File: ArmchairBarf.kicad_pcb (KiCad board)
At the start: 2 copper layers, 33 x 20.3 mm, 12 parts, among them J1 Conn_01x03_Socket, U1 WS2812-2020, U2 WS2812-2020, U3 WS2812-2020, U4 WS2812-2020, U5 WS2812-2020, U6 WS2812-2020, U7 WS2812-2020, U8 WS2812-2020, U9 WS2812-2020

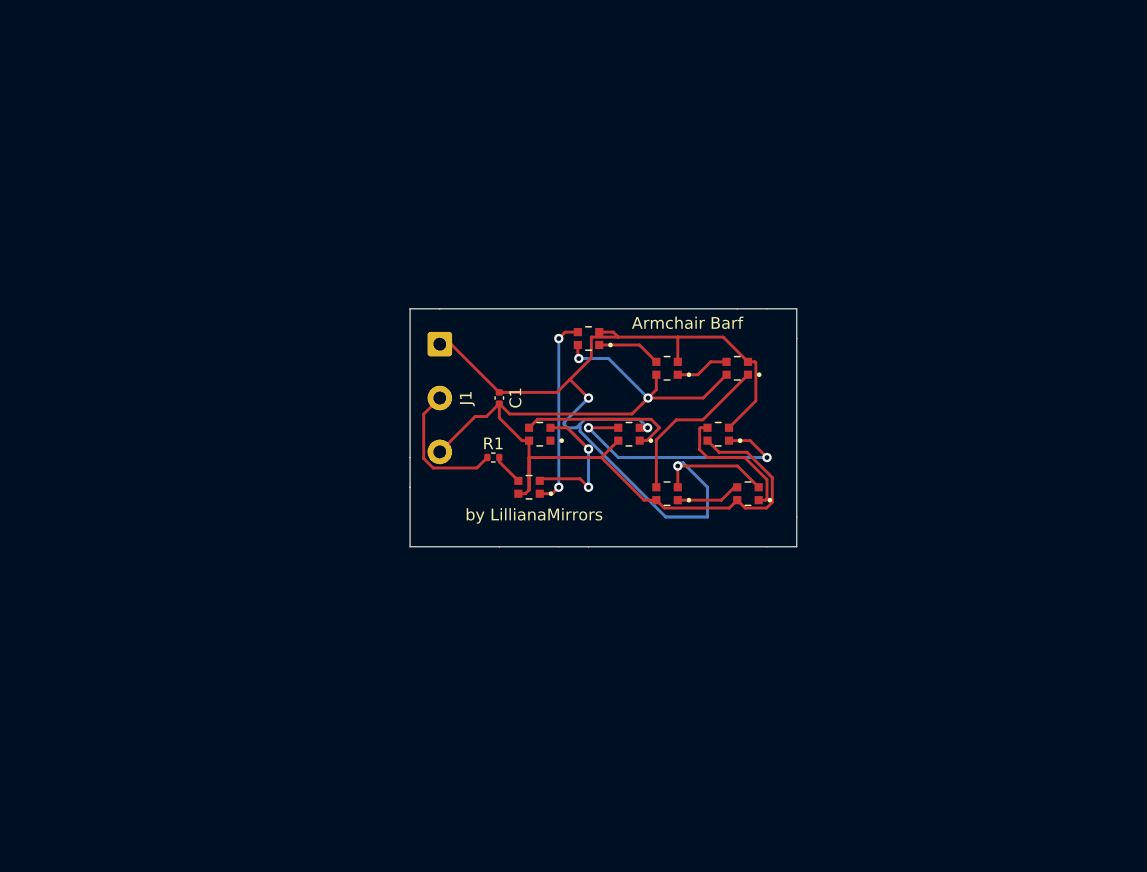
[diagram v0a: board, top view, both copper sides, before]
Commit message: Cleaned up and made proper connections and repinned to hartk's suggestions
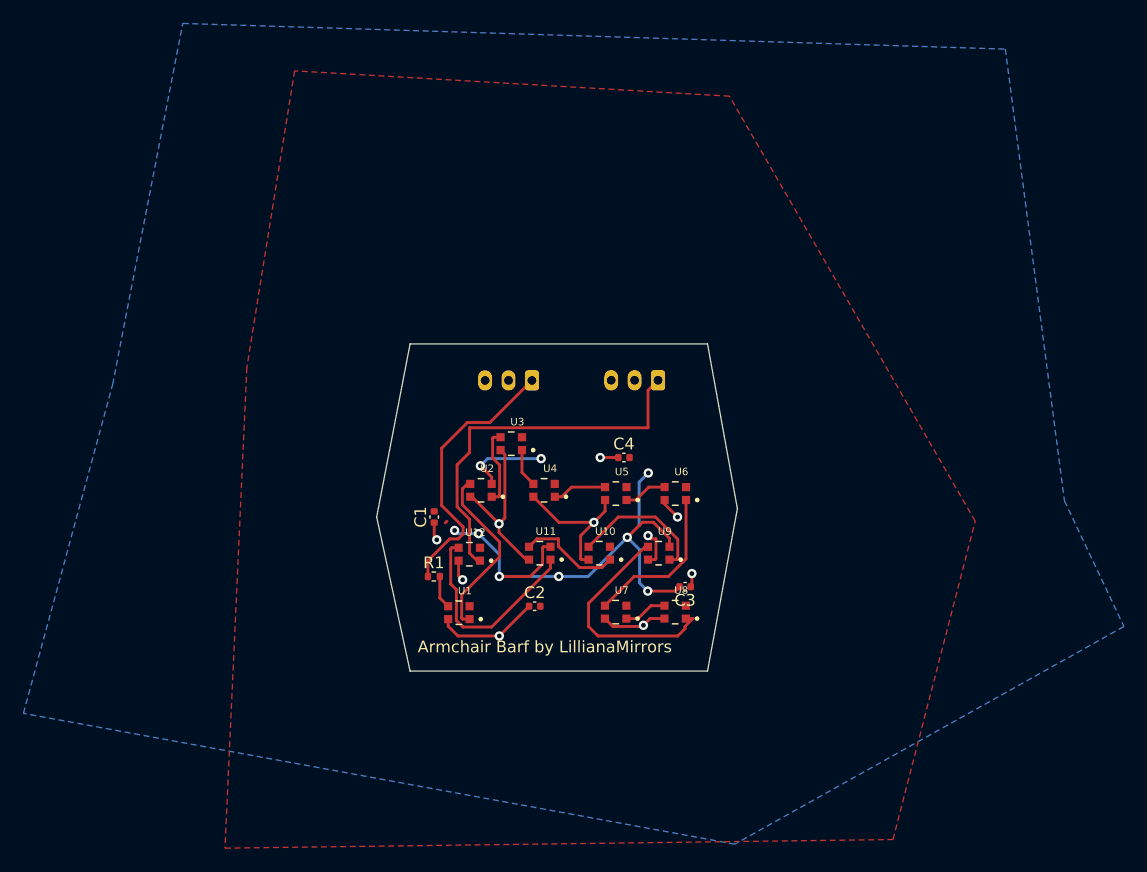
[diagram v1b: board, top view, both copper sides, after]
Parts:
- added C2: C, Capacitor_SMD:C_0402_1005Metric, F.Cu at (163.0, 111.8)
- added C3: C, Capacitor_SMD:C_0402_1005Metric, F.Cu at (175.9, 110.1)
- added C4: C, Capacitor_SMD:C_0402_1005Metric, F.Cu at (170.7, 99.1)
- added J2: Conn_01x03_Socket, Connector_JST:JST_PH_B3B-PH-K_1x03_P2.00mm_Vertical, B.Cu at (173.6, 92.5)
- added U10: WS2812-2020, WS2812-2020:LED_WS2812-2020, F.Cu at (168.6, 107.2)
- added U11: WS2812-2020, WS2812-2020:LED_WS2812-2020, F.Cu at (163.5, 107.2)
- added U12: WS2812-2020, WS2812-2020:LED_WS2812-2020, F.Cu at (157.5, 107.3)
- J1: footprint Connector_Wire:SolderWire-0.5sqmm_1x03_P4.6mm_D0.9mm_OD2.1mm -> Connector_JST:JST_PH_B3B-PH-K_1x03_P2.00mm_Vertical; moved to B.Cu
- moved U4 19.5 mm to (163.8, 101.9)
- moved U7 17.5 mm to (170.0, 112.3)
- moved U2 15.9 mm to (158.5, 101.9)
- moved U8 15.7 mm to (175.0, 112.3)
- moved U3 14.8 mm to (161.0, 97.9)
- moved U9 14.4 mm to (173.6, 107.2)
- moved U1 12.3 mm to (156.6, 112.3)
- moved C1 11.6 mm to (154.5, 104.1)
- moved R1 11.4 mm to (154.4, 109.2)
- moved J1 8.45 mm to (162.8, 92.5), turned to 180 degrees
- moved U6 6.21 mm to (175.0, 102.1)
- moved U5 4.38 mm to (170.0, 102.1)
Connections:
- net Net-(J1-Pin_3) renamed +5V
- C1 pad 2: Net-(J1-Pin_1) -> GND
- J1 pad 2: Net-(J1-Pin_2) -> GND
- R1 pad 1: Net-(J1-Pin_2) -> Net-(J1-Pin_1)
- U1 pad 2: Net-(J1-Pin_1) -> GND
- U2 pad 2: Net-(J1-Pin_1) -> GND
- U3 pad 2: Net-(J1-Pin_1) -> GND
- U4 pad 2: Net-(J1-Pin_1) -> GND
- U5 pad 2: Net-(J1-Pin_1) -> GND
- U6 pad 2: Net-(J1-Pin_1) -> GND
- U7 pad 2: Net-(J1-Pin_1) -> GND
- U8 pad 2: Net-(J1-Pin_1) -> GND
- U9 pad 1: unconnected-(U9-DO-Pad1) -> Net-(U10-DI)
- U9 pad 2: Net-(J1-Pin_1) -> GND
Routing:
- net Net-(J1-Pin_1): track 101.5 -> 23.5 mm, vias 5 -> 0
- net GND: track 0.00 -> 52.5 mm, vias 0 -> 9
- net +5V: track 85.6 -> 52.7 mm, vias 2 -> 10
- net Net-(J2-Pin_1): track 0.00 -> 32.4 mm
- net Net-(U7-DO): track 22.7 -> 3.71 mm, vias 2 -> 0
- net Net-(U11-DO): track 0.00 -> 18.1 mm
- net Net-(J1-Pin_2): track 11.9 -> 0.00 mm
- net Net-(U10-DI): track 0.00 -> 11.8 mm
- net Net-(U4-DO): track 14.2 -> 4.64 mm
- net Net-(U10-DO): track 0.00 -> 8.86 mm
- net Net-(U8-DO): track 13.9 -> 19.6 mm
- net Net-(U6-DO): track 11.7 -> 13.6 mm
- net Net-(U5-DO): track 5.54 -> 3.71 mm
- net Net-(U3-DO): track 4.62 -> 3.29 mm
- net Net-(U1-DO): track 16.4 -> 15.3 mm, vias 2 -> 0
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- added copper zone on B.Cu, net +5V
- added copper zone on F.Cu, net GND
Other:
- board size 33 x 20.3 mm -> 30.8 x 27.9 mm
- board text added: "Armchair Barf by LillianaMirrors"
- board text added: "DO|GND|+5V"
- board text added: "Di|GND|+5V"
- board text removed: "Armchair Barf"
- board text removed: "by LillianaMirrors"

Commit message: Redesigned for Whopping's Rainbow Barf form factor.
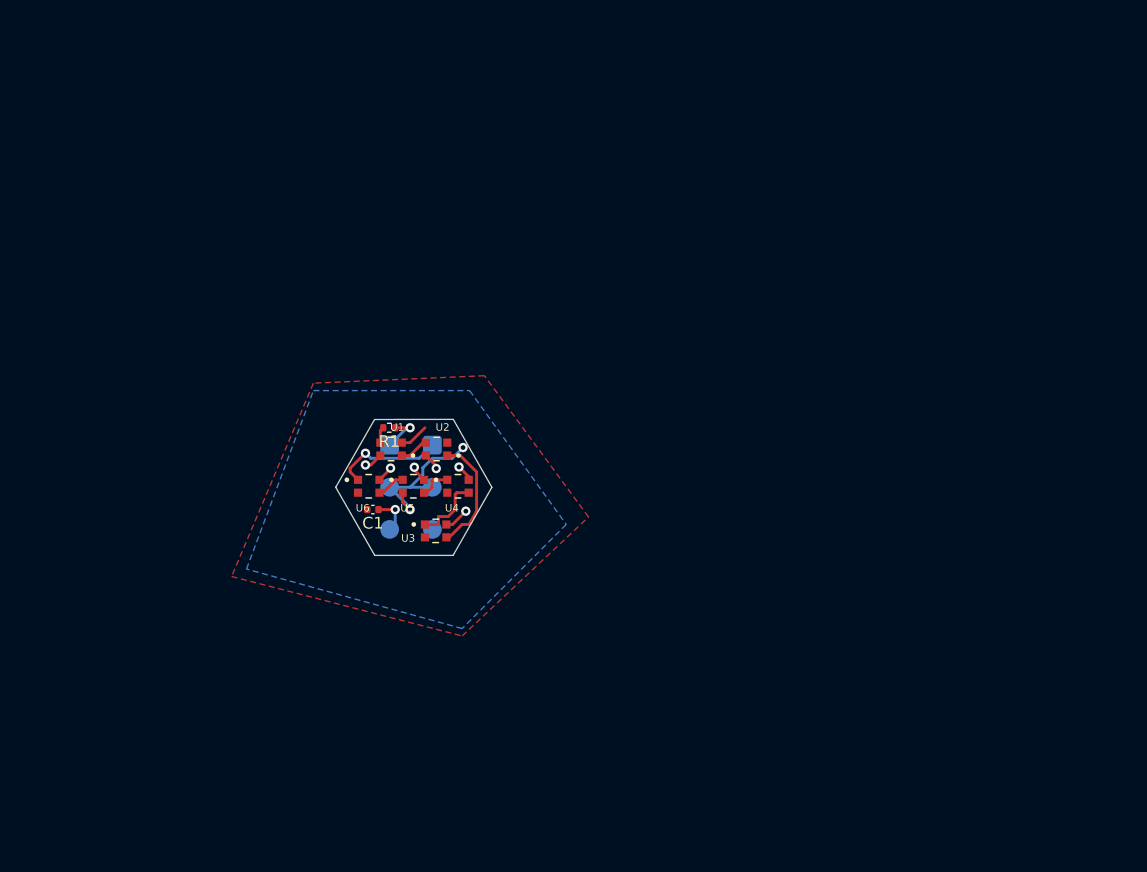
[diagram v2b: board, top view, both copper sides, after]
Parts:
- removed C2, C3, C4: C, Capacitor_SMD:C_0402_1005Metric
- removed U10, U11, U12, U7, U8, U9: WS2812-2020, WS2812-2020:LED_WS2812-2020
- J1, J2: footprint Connector_JST:JST_PH_B3B-PH-K_1x03_P2.00mm_Vertical -> Connector_Wire:SolderWire-0.1sqmm_1x03_P3.6mm_D0.4mm_OD1mm
- moved U6 26.2 mm to (148.9, 101.5), turned to 180 degrees
- moved J2 20.0 mm to (154.3, 98.0), turned to -90 degrees
- moved U5 17.3 mm to (152.7, 101.5), turned to 180 degrees
- moved U1 15.1 mm to (150.8, 98.3)
- moved J1 13.3 mm to (150.7, 98.0), turned to -90 degrees
- moved R1 13.3 mm to (150.6, 96.5), turned to 180 degrees
- moved U3 9.86 mm to (154.6, 105.3), turned to 180 degrees
- moved U4 7.36 mm to (156.5, 101.5), turned to 180 degrees
- moved C1 5.27 mm to (149.2, 103.5), turned to 180 degrees
- moved U2 5.18 mm to (154.7, 98.3)
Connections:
- U6 pad 1: Net-(U6-DO) -> Net-(J2-Pin_1)
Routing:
- net +5V: track 52.7 -> 12.8 mm, vias 10 -> 7
- net GND: track 52.5 -> 16.7 mm, vias 9 -> 2
- net Net-(J2-Pin_1): track 32.4 -> 9.47 mm, vias 0 -> 1
- net Net-(J1-Pin_1): track 23.5 -> 3.63 mm, vias 0 -> 1
- net Net-(U8-DO): track 19.6 -> 0.00 mm
- net Net-(U11-DO): track 18.1 -> 0.00 mm
- net Net-(U6-DO): track 13.6 -> 0.00 mm
- net Net-(U1-DO): track 15.3 -> 2.51 mm
- net Net-(U10-DI): track 11.8 -> 0.00 mm
- net Net-(U10-DO): track 8.86 -> 0.00 mm
- net Net-(U7-DO): track 3.71 -> 0.00 mm
- net Net-(U2-DO): track 6.59 -> 10.1 mm
- net Net-(U3-DO): track 3.29 -> 6.02 mm
- net Net-(U4-DO): track 4.64 -> 2.80 mm
- net Net-(U1-DI): track 2.83 -> 1.37 mm
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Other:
- board size 30.8 x 27.9 mm -> 13.3 x 11.6 mm
- board text removed: "Armchair Barf by LillianaMirrors"
- board text removed: "DO|GND|+5V"
- board text removed: "Di|GND|+5V"
